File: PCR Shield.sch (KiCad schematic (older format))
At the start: 13 parts

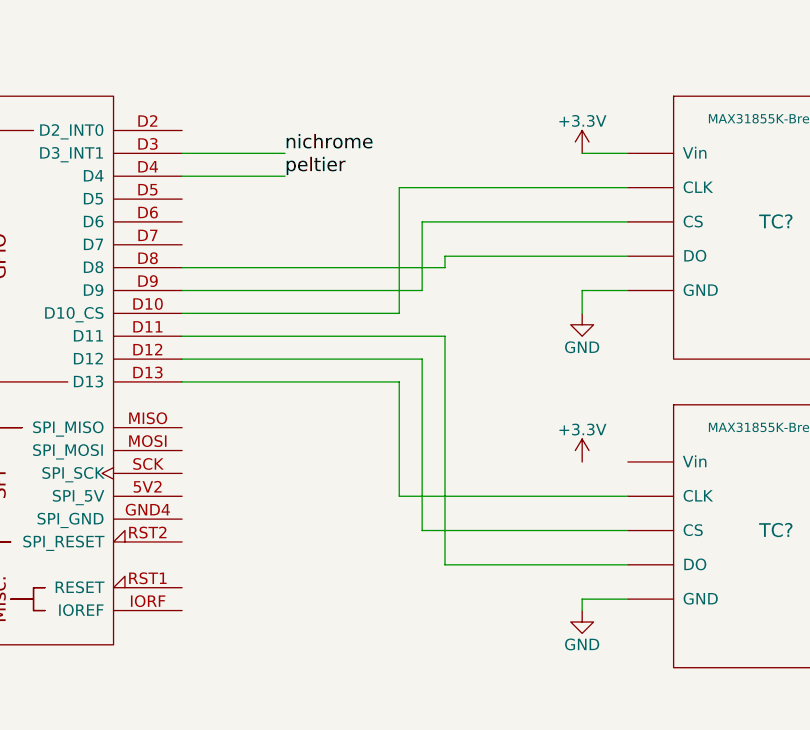
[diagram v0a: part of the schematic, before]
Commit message: Updated wire reference to make the schematic more readable
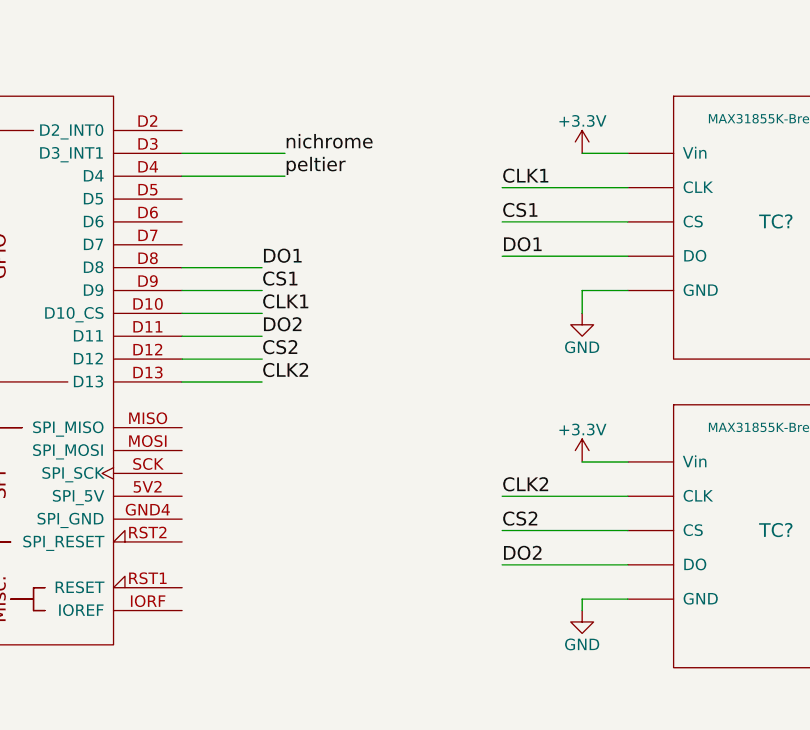
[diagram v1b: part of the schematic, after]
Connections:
- net +3V3: now also TC?.~ (Vin)
- net CLK1: now reaches ARD?.D10 (D10_CS), TC?.~ (Vin)
- net DO2: now reaches ARD?.D11, TC?.~ (Vin)
- net CS2: now reaches ARD?.D12, TC?.~ (Vin)
- net CLK2: now reaches ARD?.D13, TC?.~ (Vin)
- net DO1: now reaches ARD?.D8, TC?.~ (Vin)
- net CS1: now reaches ARD?.D9, TC?.~ (Vin)
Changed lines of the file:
@@
 LIBS:contrib
 LIBS:valves
-LIBS:arduino
 LIBS:PCR Shield-cache
 EELAYER 25 0
@@
 $EndComp
 Wire Wire Line
-	5350 4900 6300 4900
-Wire Wire Line
-	6300 4900 6300 5400
-Wire Wire Line
-	6300 5400 7300 5400
-Wire Wire Line
-	5350 4800 6400 4800
-Wire Wire Line
-	6400 4800 6400 5550
-Wire Wire Line
-	6400 5550 7300 5550
-Wire Wire Line
-	5350 4700 6500 4700
-Wire Wire Line
-	6500 4700 6500 5700
-Wire Wire Line
-	6500 5700 7300 5700
-Wire Wire Line
-	5350 4600 6300 4600
-Wire Wire Line
-	6300 4600 6300 4050
-Wire Wire Line
-	6300 4050 7300 4050
-Wire Wire Line
-	5350 4500 6400 4500
-Wire Wire Line
-	6400 4500 6400 4200
-Wire Wire Line
-	6400 4200 7300 4200
-Wire Wire Line
-	5350 4400 6500 4400
-Wire Wire Line
-	6500 4400 6500 4350
-Wire Wire Line
-	6500 4350 7300 4350
-Wire Wire Line
 	5350 4000 5800 4000
 Wire Wire Line
@@
 Wire Wire Line
 	7300 3900 7100 3900
+Wire Wire Line
+	7100 5250 7300 5250
+Text Label 5700 4400 0    60   ~ 0
+DO1
+Text Label 5700 4500 0    60   ~ 0
+CS1
+Text Label 5700 4600 0    60   ~ 0
+CLK1
+Text Label 5700 4700 0    60   ~ 0
+DO2
+Text Label 5700 4800 0    60   ~ 0
+CS2
+Text Label 5700 4900 0    60   ~ 0
+CLK2
+Wire Wire Line
+	5350 4400 5700 4400
+Wire Wire Line
+	5350 4500 5700 4500
+Wire Wire Line
+	5350 4600 5700 4600
+Wire Wire Line
+	5350 4700 5700 4700
+Wire Wire Line
+	5350 4800 5700 4800
+Wire Wire Line
+	5350 4900 5700 4900
+Wire Wire Line
+	7300 4050 6750 4050
+Wire Wire Line
+	7300 4200 6750 4200
+Wire Wire Line
+	7300 4350 6750 4350
+Wire Wire Line
+	7300 5400 6750 5400
+Wire Wire Line
+	7300 5550 6750 5550
+Wire Wire Line
+	7300 5700 6750 5700
+Text Label 6750 4050 0    60   ~ 0
+CLK1
+Text Label 6750 4200 0    60   ~ 0
+CS1
+Text Label 6750 4350 0    60   ~ 0
+DO1
+Text Label 6750 5400 0    60   ~ 0
+CLK2
+Text Label 6750 5550 0    60   ~ 0
+CS2
+Text Label 6750 5700 0    60   ~ 0
+DO2
 $EndSCHEMATC

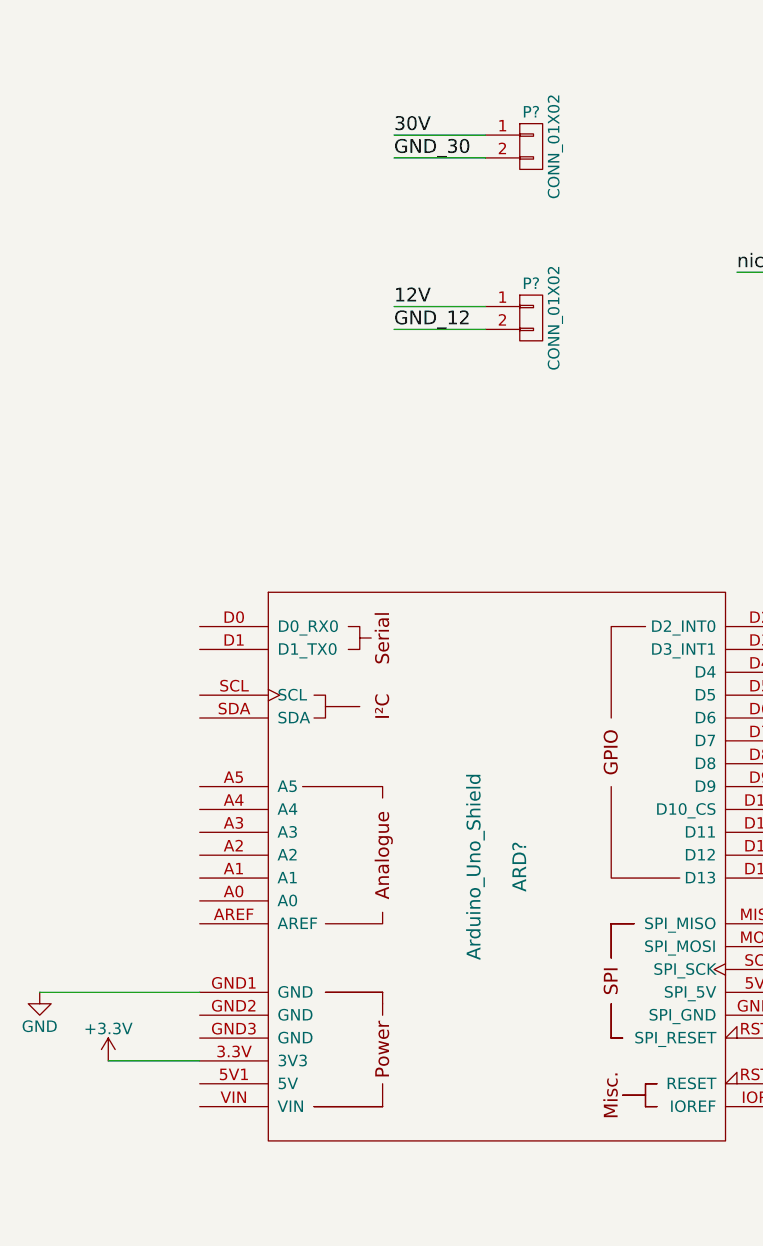
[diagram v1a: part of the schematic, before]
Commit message: Added the fan information
Figured out the crazy power supply requirements and added them onto the
readme
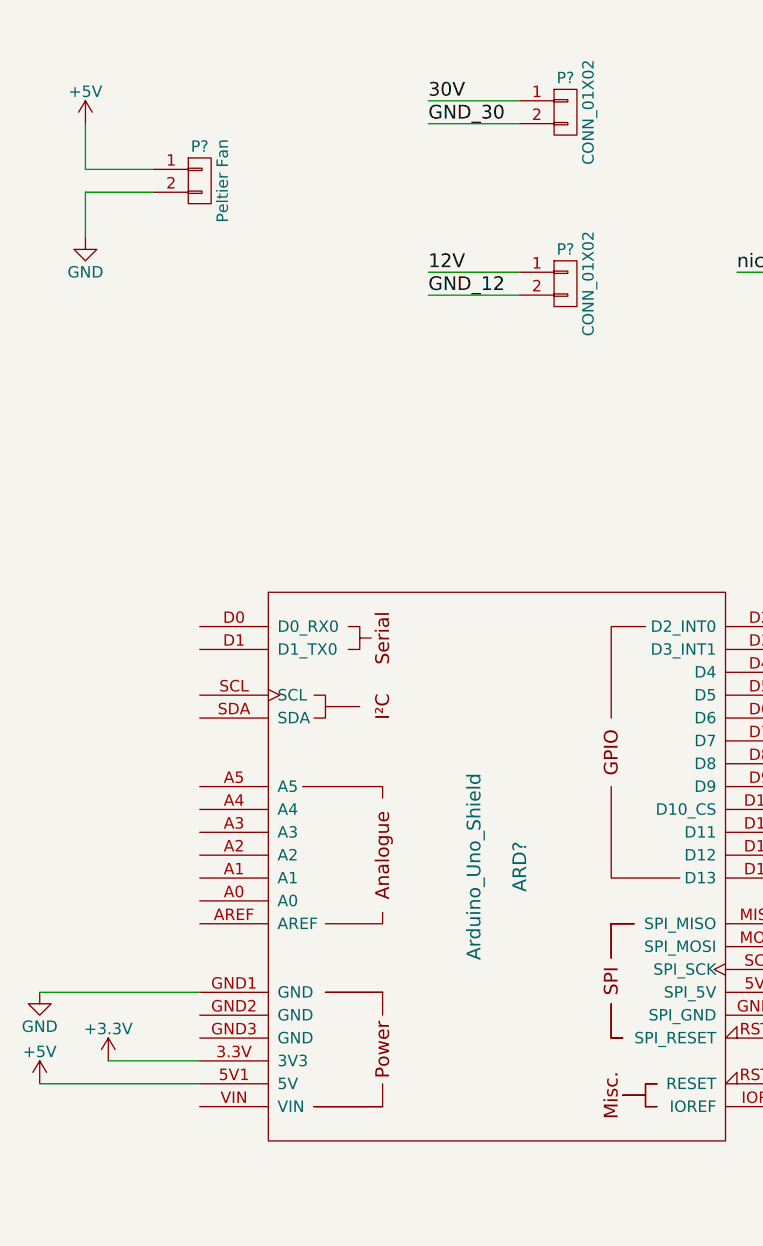
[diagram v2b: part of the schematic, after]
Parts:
- added P?: Peltier Fan, symbol CONN_01X02
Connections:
- net GND: now also P?.2 (P2)
- net +5V: now reaches ARD?.5V1 (5V)
- net +5V: now also P?.1 (P1)
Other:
- moved on the sheet: P?
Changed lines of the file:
@@
 L CONN_01X02 P?
 U 1 1 5A338B64
-P 4200 1700
-F 0 "P?" H 4200 1850 50  0000 C CNN
-F 1 "CONN_01X02" V 4300 1700 50  0000 C CNN
-F 2 "" H 4200 1700 50  0000 C CNN
-F 3 "" H 4200 1700 50  0000 C CNN
-	1    4200 1700
+P 4350 1550
+F 0 "P?" H 4350 1700 50  0000 C CNN
+F 1 "CONN_01X02" V 4450 1550 50  0000 C CNN
+F 2 "" H 4350 1550 50  0000 C CNN
+F 3 "" H 4350 1550 50  0000 C CNN
+	1    4350 1550
 	1    0    0    -1
 $EndComp
@@
 L CONN_01X02 P?
 U 1 1 5A338BAE
-P 4200 2450
-F 0 "P?" H 4200 2600 50  0000 C CNN
-F 1 "CONN_01X02" V 4300 2450 50  0000 C CNN
-F 2 "" H 4200 2450 50  0000 C CNN
-F 3 "" H 4200 2450 50  0000 C CNN
-	1    4200 2450
-	1    0    0    -1
-$EndComp
-Text Label 3600 1650 0    60   ~ 0
+P 4350 2300
+F 0 "P?" H 4350 2450 50  0000 C CNN
+F 1 "CONN_01X02" V 4450 2300 50  0000 C CNN
+F 2 "" H 4350 2300 50  0000 C CNN
+F 3 "" H 4350 2300 50  0000 C CNN
+	1    4350 2300
+	1    0    0    -1
+$EndComp
+Text Label 3750 1500 0    60   ~ 0
 30V
-Text Label 3600 1750 0    60   ~ 0
+Text Label 3750 1600 0    60   ~ 0
 GND_30
-Text Label 3600 2400 0    60   ~ 0
+Text Label 3750 2250 0    60   ~ 0
 12V
-Text Label 3600 2500 0    60   ~ 0
+Text Label 3750 2350 0    60   ~ 0
 GND_12
 Text Notes 7900 6850 0    60   ~ 0
@@
 Connection ~ 8100 2000
 Wire Wire Line
-	4000 1650 3600 1650
-Wire Wire Line
-	4000 1750 3600 1750
-Wire Wire Line
-	4000 2400 3600 2400
-Wire Wire Line
-	4000 2500 3600 2500
+	4150 1500 3750 1500
+Wire Wire Line
+	4150 1600 3750 1600
+Wire Wire Line
+	4150 2250 3750 2250
+Wire Wire Line
+	4150 2350 3750 2350
 Wire Wire Line
 	7700 2350 7700 2250
@@
 Text Label 6750 5700 0    60   ~ 0
 DO2
+$Comp
+L +5V #PWR?
+U 1 1 5A348AD9
+P 2050 5800
+F 0 "#PWR?" H 2050 5650 50  0001 C CNN
+F 1 "+5V" H 2050 5940 50  0000 C CNN
+F 2 "" H 2050 5800 50  0000 C CNN
+F 3 "" H 2050 5800 50  0000 C CNN
+	1    2050 5800
+	1    0    0    -1
+$EndComp
+Wire Wire Line
+	2050 5800 2750 5800
+$Comp
+L +5V #PWR?
+U 1 1 5A348B64
+P 2250 1600
+F 0 "#PWR?" H 2250 1450 50  0001 C CNN
+F 1 "+5V" H 2250 1740 50  0000 C CNN
+F 2 "" H 2250 1600 50  0000 C CNN
+F 3 "" H 2250 1600 50  0000 C CNN
+	1    2250 1600
+	1    0    0    -1
+$EndComp
+$Comp
+L GND #PWR?
+U 1 1 5A348BB9
+P 2250 2100
+F 0 "#PWR?" H 2250 1850 50  0001 C CNN
+F 1 "GND" H 2250 1950 50  0000 C CNN
+F 2 "" H 2250 2100 50  0000 C CNN
+F 3 "" H 2250 2100 50  0000 C CNN
+	1    2250 2100
+	1    0    0    -1
+$EndComp
+$Comp
+L CONN_01X02 P?
+U 1 1 5A348C1B
+P 2750 1850
+F 0 "P?" H 2750 2000 50  0000 C CNN
+F 1 "Peltier Fan" V 2850 1850 50  0000 C CNN
+F 2 "" H 2750 1850 50  0000 C CNN
+F 3 "" H 2750 1850 50  0000 C CNN
+	1    2750 1850
+	1    0    0    -1
+$EndComp
+Wire Wire Line
+	2250 1600 2250 1800
+Wire Wire Line
+	2250 1800 2550 1800
+Wire Wire Line
+	2250 2100 2250 1900
+Wire Wire Line
+	2250 1900 2550 1900
 $EndSCHEMATC
